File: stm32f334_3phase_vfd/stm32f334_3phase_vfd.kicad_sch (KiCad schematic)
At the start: 0 parts

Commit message: continue schematic work
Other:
- added sheet CPU (cpu.kicad_sch)
- sheet power ports: added 3V3_DIG, 3V3_ISENS, EM_STOP, HV, HinU, HinV, HinW, I_A, I_B, I_C, LinU, LinV, LinW, OUTPUT_PHA, OUTPUT_PHB, OUTPUT_PHC, T1, T2, Tso, VCC_15V; removed none

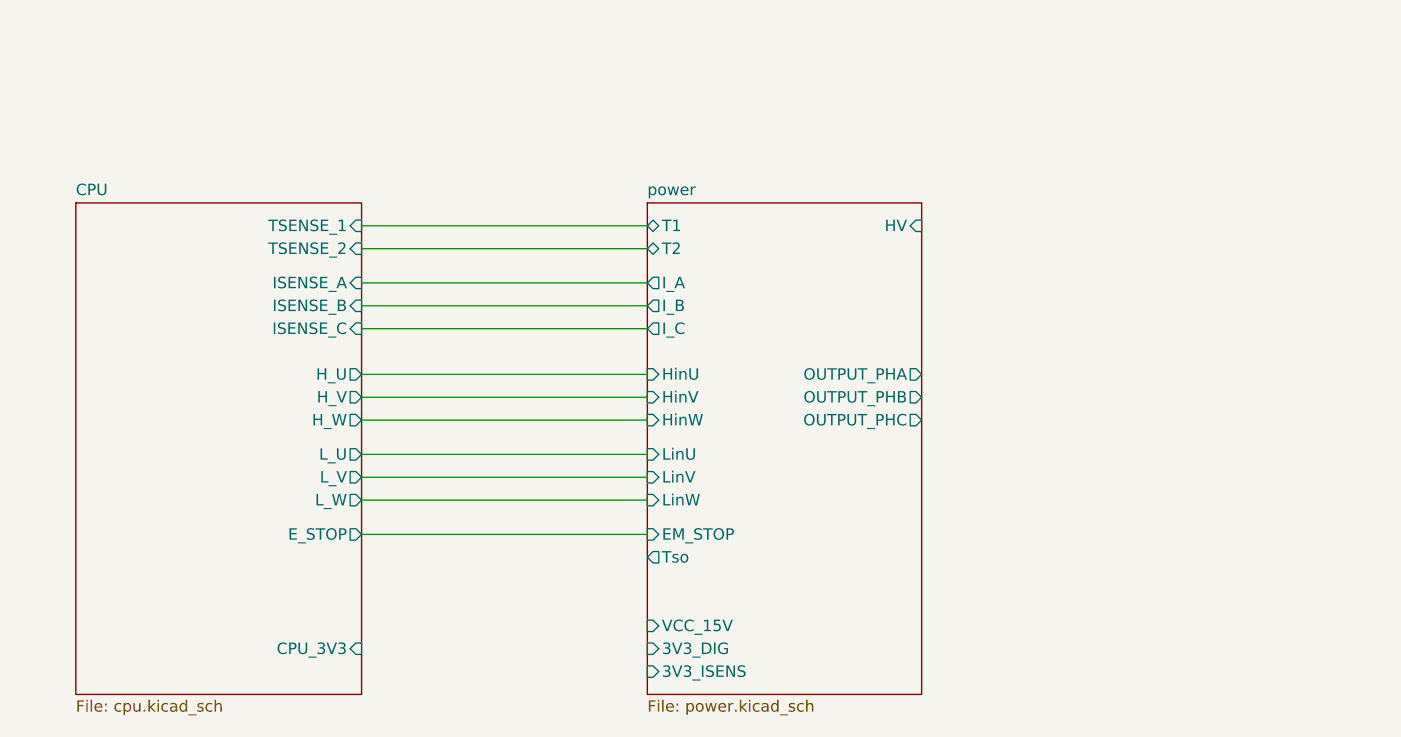
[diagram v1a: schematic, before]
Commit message: update schematic
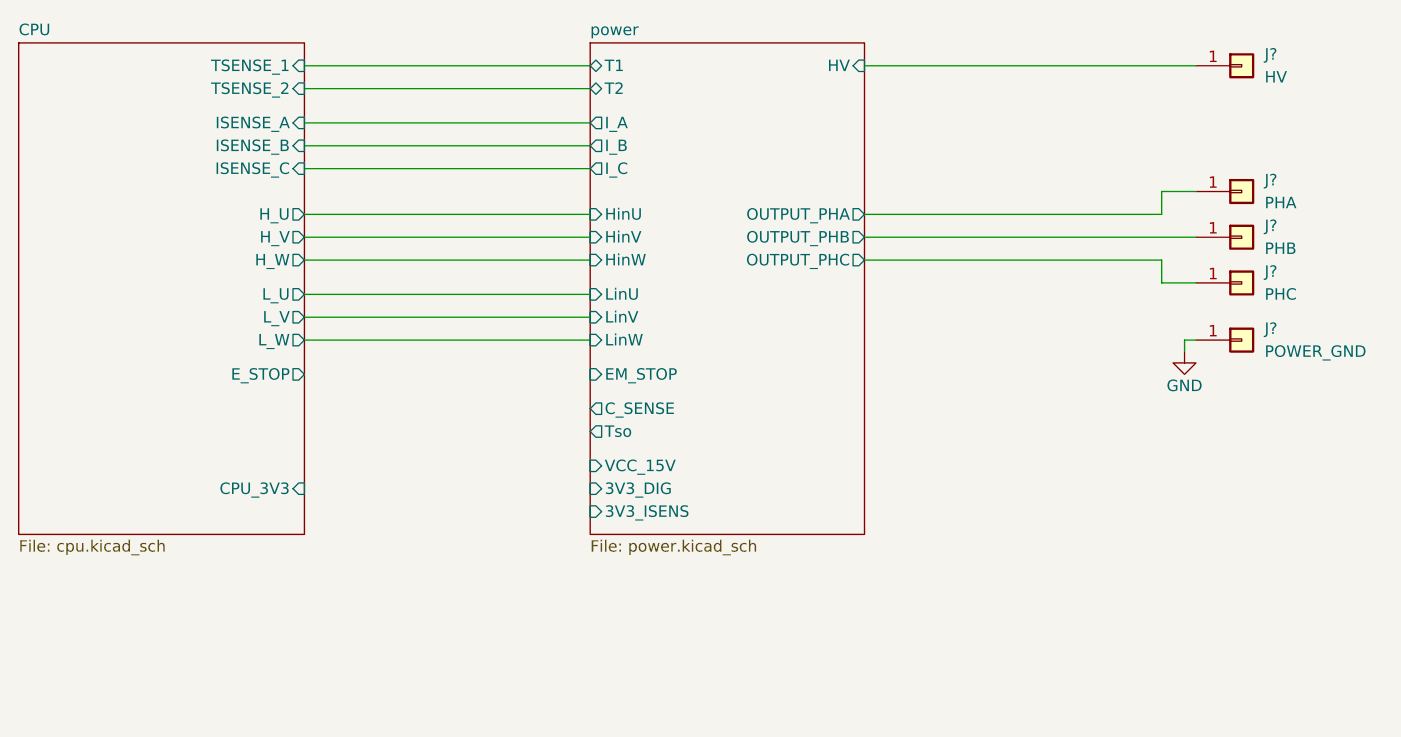
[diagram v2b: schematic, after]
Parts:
- added J?: PHB, symbol Connector_Generic:Conn_01x01
- added J?: PHA, symbol Connector_Generic:Conn_01x01
- added J?: HV, symbol Connector_Generic:Conn_01x01
- added J?: PHC, symbol Connector_Generic:Conn_01x01
- added J?: POWER_GND, symbol Connector_Generic:Conn_01x01
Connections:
- net power/HV: now also J?.1 (Pin_1)
- net power/OUTPUT_PHA: now also J?.1 (Pin_1)
- net power/OUTPUT_PHB: now also J?.1 (Pin_1)
- net power/OUTPUT_PHC: now also J?.1 (Pin_1)
- new net GND: J?.1 (Pin_1)
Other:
- sheet power ports: added C_SENSE; removed none

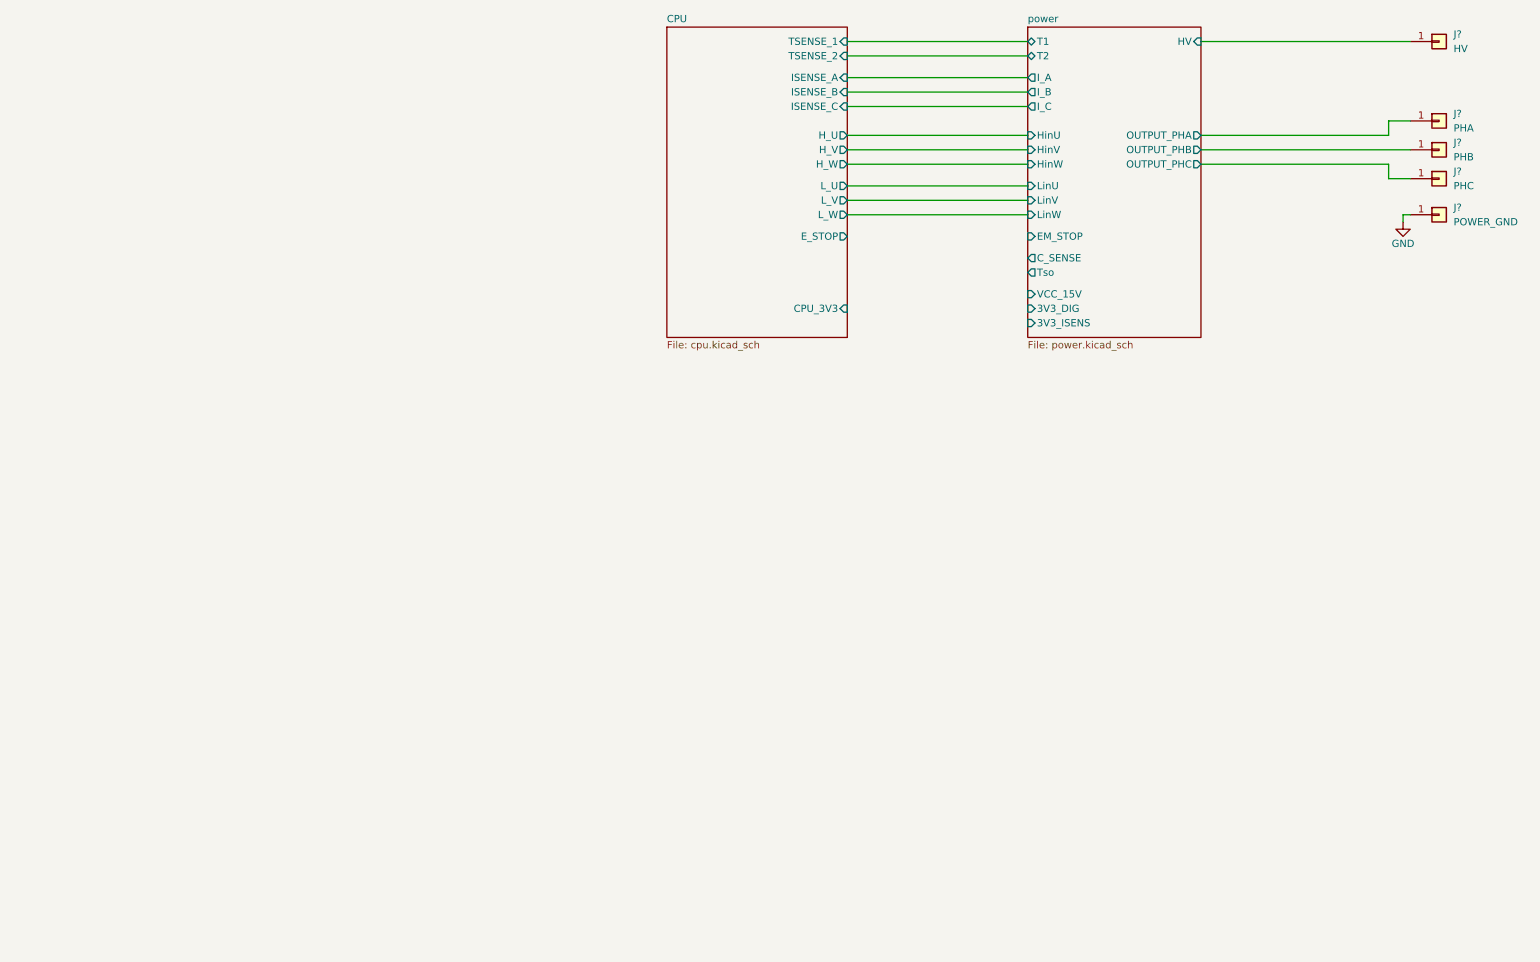
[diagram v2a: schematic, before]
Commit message: update schematic, start power section layout
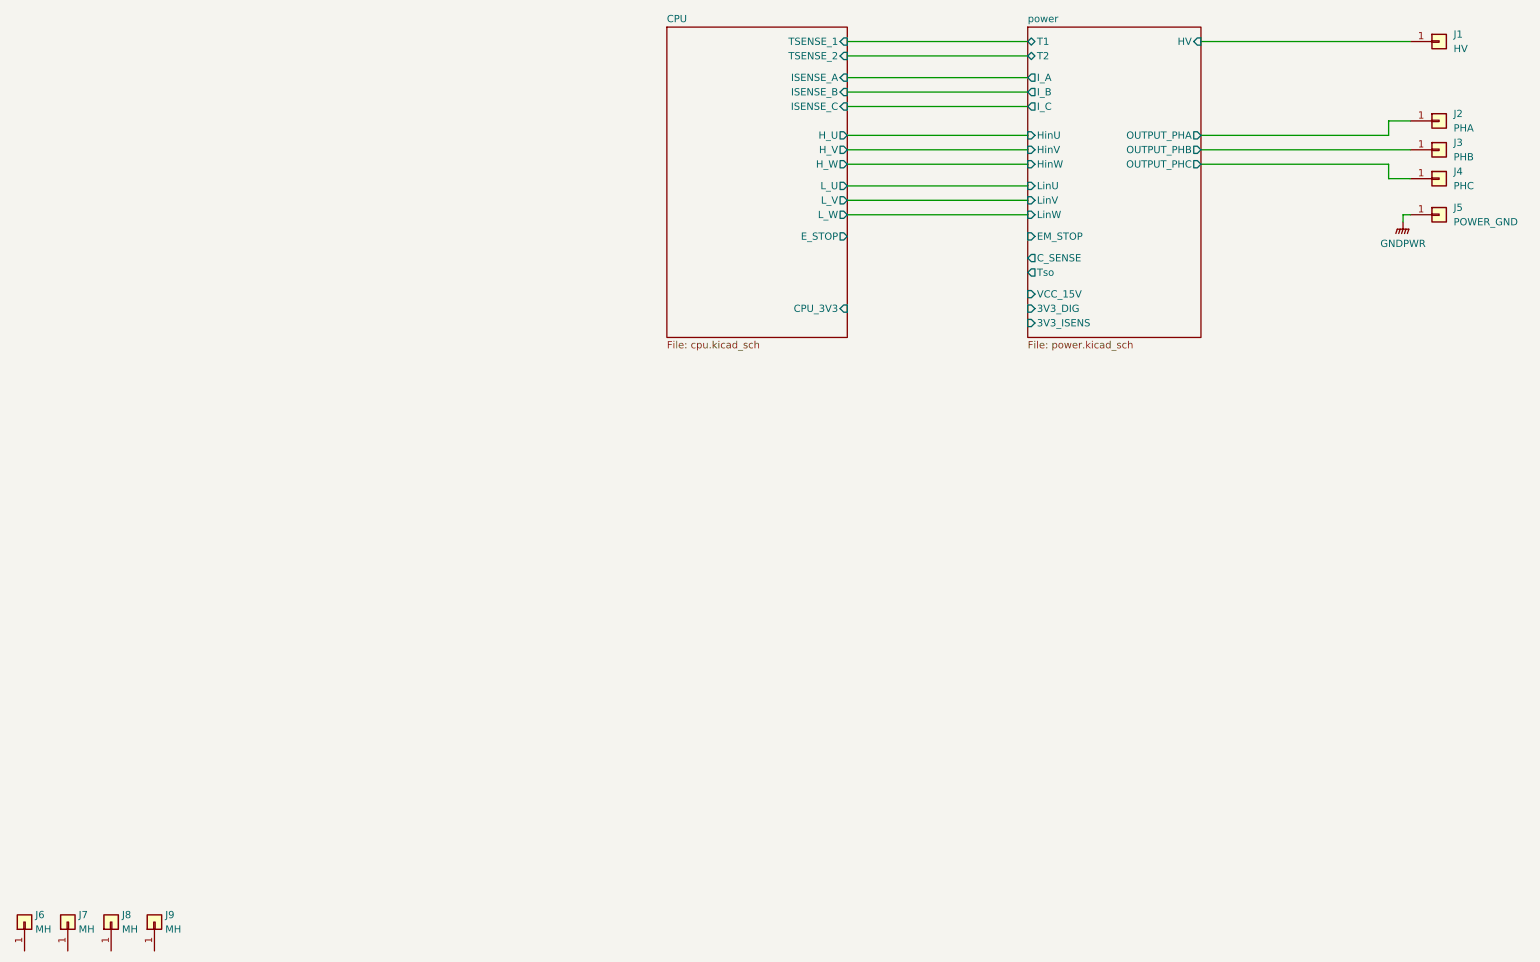
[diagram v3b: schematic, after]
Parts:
- added J6, J7, J8, J9: MH, MountingHole:MountingHole_3.2mm_M3_Pad_TopBottom, symbol Connector_Generic:Conn_01x01
- J1, J2, J3, J4, J5: renamed from J?; footprint (none) -> stm32f334_3phase_vfd:1904969
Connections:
- net GND renamed GNDPWR

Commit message: move 3 phase current sensors on a new board, allow for the current sense board to be stacked
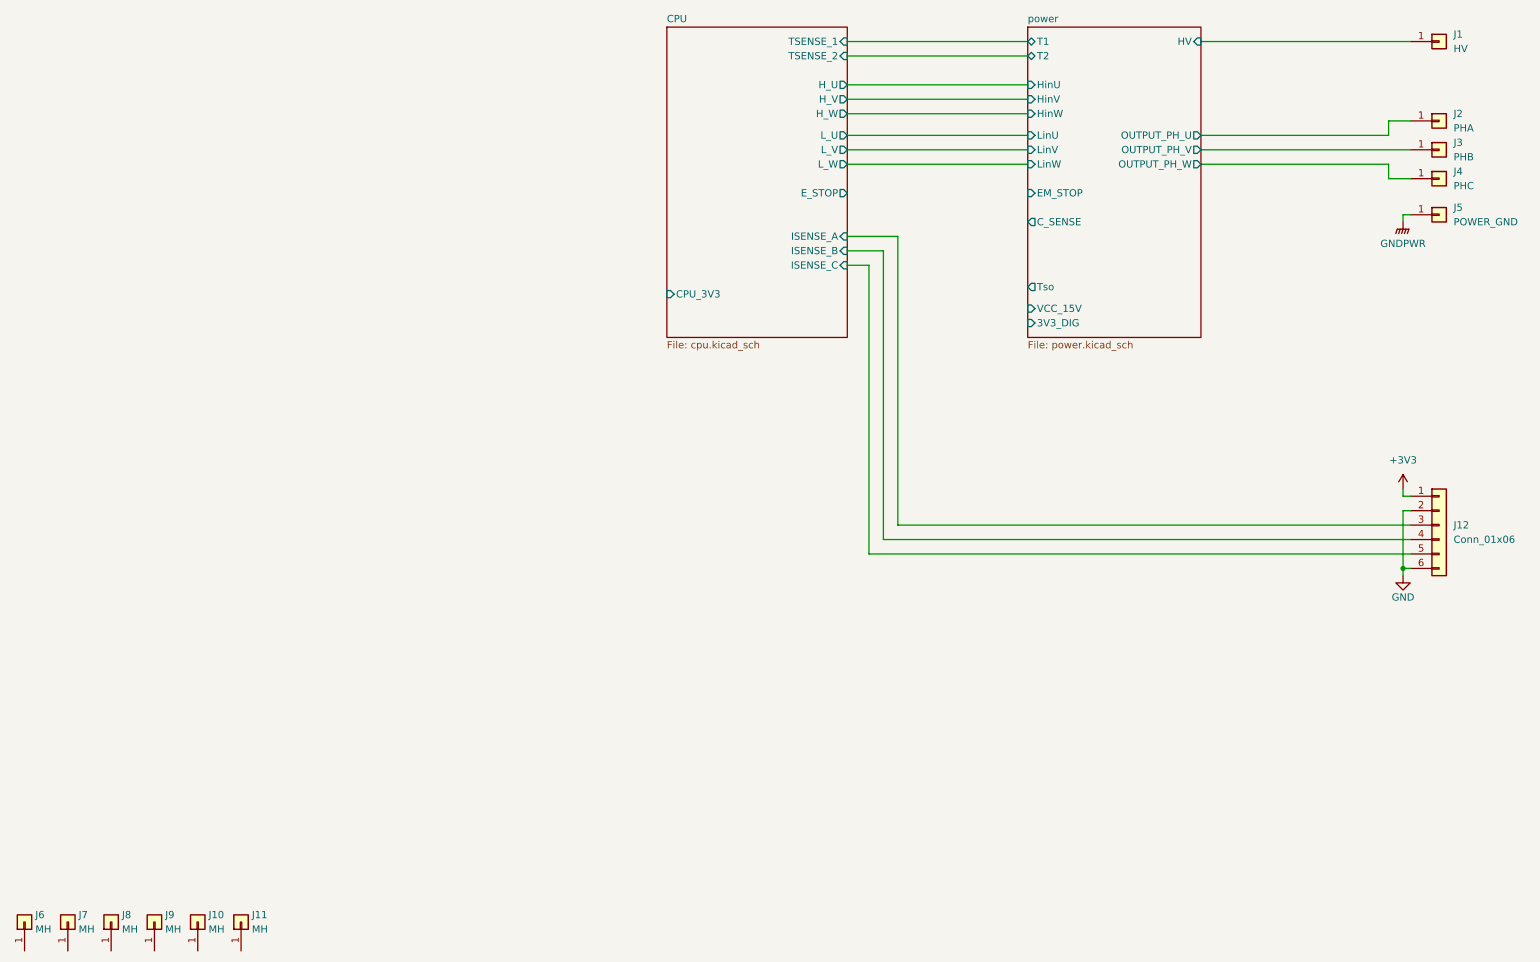
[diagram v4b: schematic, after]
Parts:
- added J10, J11: MH, MountingHole:MountingHole_3.2mm_M3_Pad_TopBottom, symbol Connector_Generic:Conn_01x01
- added J12: Conn_01x06, Connector_JST:JST_PH_B6B-PH-K_1x06_P2.00mm_Vertical, symbol Connector_Generic:Conn_01x06
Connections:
- net CPU/ISENSE_A: now also J12.3 (Pin_3)
- net CPU/ISENSE_B: now also J12.4 (Pin_4)
- net CPU/ISENSE_C: now also J12.5 (Pin_5)
- net power/OUTPUT_PHA renamed power/OUTPUT_PH_U
- net power/OUTPUT_PHB renamed power/OUTPUT_PH_V
- net power/OUTPUT_PHC renamed power/OUTPUT_PH_W
- new net +3V3: J12.1 (Pin_1)
- new net GND: J12.2 (Pin_2), J12.6 (Pin_6)
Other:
- sheet power ports: added OUTPUT_PH_U, OUTPUT_PH_V, OUTPUT_PH_W; removed 3V3_ISENS, I_A, I_B, I_C, OUTPUT_PHA, OUTPUT_PHB, OUTPUT_PHC

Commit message: switch to LQFP48 cpu, continue workin on layout
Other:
- sheet CPU ports: added C_SENSE; removed none
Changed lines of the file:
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@@
+    (stroke (width 0) (type default) (color 0 0 0 0))
+  )
+  (wire (pts (xy 163.83 53.34) (xy 195.58 53.34))
     (stroke (width 0) (type default) (color 0 0 0 0))
   )
@@
   (symbol (lib_id "power:+3V3") (at 261.62 100.33 0) (unit 1)
     (in_bom yes) (on_board yes) (fields_autoplaced)
-    (property "Reference" "#PWR?" (id 0) (at 261.62 104.14 0)
+    (property "Reference" "#PWR0108" (id 0) (at 261.62 104.14 0)
       (effects (font (size 1.27 1.27)) hide)
     )
@@
   (symbol (lib_id "power:GND") (at 261.62 115.57 0) (unit 1)
     (in_bom yes) (on_board yes)
-    (property "Reference" "#PWR?" (id 0) (at 261.62 121.92 0)
+    (property "Reference" "#PWR0109" (id 0) (at 261.62 121.92 0)
       (effects (font (size 1.27 1.27)) hide)
     )
@@
       (effects (font (size 1.27 1.27)) (justify right))
     )
+    (pin "C_SENSE" input (at 163.83 53.34 0)
+      (effects (font (size 1.27 1.27)) (justify right))
+    )
   )
   (sheet (at 195.58 19.05) (size 30.48 54.61) (fields_autoplaced)
@@
       (reference "#PWR0107") (unit 1) (value "GNDPWR") (footprint "")
     )
+    (path "/5688ef43-203d-42fa-8968-6c89131b4954"
+      (reference "#PWR0108") (unit 1) (value "+3V3") (footprint "")
+    )
+    (path "/ae8a7779-a204-40cc-a9a9-a5e8072c90c1"
+      (reference "#PWR0109") (unit 1) (value "GND") (footprint "")
+    )
+    (path "/6800bd5f-b25d-4977-8025-22368615975a/f68bf9a1-24c8-4c89-a68f-af7873d40121"
+      (reference "#PWR0110") (unit 1) (value "GND") (footprint "")
+    )
+    (path "/6800bd5f-b25d-4977-8025-22368615975a/08694d45-d770-4503-891f-e08473ebf295"
+      (reference "#PWR0111") (unit 1) (value "GND") (footprint "")
+    )
+    (path "/6800bd5f-b25d-4977-8025-22368615975a/ed269b40-9264-4042-b7e9-e49ce5a16a75"
+      (reference "#PWR0112") (unit 1) (value "GND") (footprint "")
+    )
+    (path "/6800bd5f-b25d-4977-8025-22368615975a/e9d903db-c5d7-444d-9c1e-bcca6f38ba00"
+      (reference "#PWR0113") (unit 1) (value "GND") (footprint "")
+    )
+    (path "/6800bd5f-b25d-4977-8025-22368615975a/c09010e8-cc9e-417f-b671-a1bfb5ab756d"
+      (reference "#PWR0114") (unit 1) (value "GND") (footprint "")
+    )
+    (path "/6800bd5f-b25d-4977-8025-22368615975a/f398151a-e08f-48fe-877f-4d66b9143ea6"
+      (reference "#PWR0115") (unit 1) (value "GND") (footprint "")
+    )
     (path "/aa6cee37-2fbc-47dd-b076-5b892a0ca157/9c4d5739-f999-44ba-9a82-45aeae16f88b"
       (reference "#PWR0201") (unit 1) (value "GND") (footprint "")
@@
       (reference "#PWR0223") (unit 1) (value "GNDPWR") (footprint "")
     )
-    (path "/5688ef43-203d-42fa-8968-6c89131b4954"
-      (reference "#PWR?") (unit 1) (value "+3V3") (footprint "")
-    )
-    (path "/ae8a7779-a204-40cc-a9a9-a5e8072c90c1"
-      (reference "#PWR?") (unit 1) (value "GND") (footprint "")
-    )
     (path "/6800bd5f-b25d-4977-8025-22368615975a/bb28fcff-49cf-47f9-96e8-a400a50b783f"
-      (reference "C101") (unit 1) (value "12p") (footprint "")
+      (reference "C101") (unit 1) (value "8p") (footprint "Capacitor_SMD:C_0805_2012Metric")
     )
     (path "/6800bd5f-b25d-4977-8025-22368615975a/3e6e72e2-2939-4642-a839-c8855147206b"
-      (reference "C102") (unit 1) (value "12p") (footprint "")
+      (reference "C102") (unit 1) (value "8p") (footprint "Capacitor_SMD:C_0805_2012Metric")
     )
     (path "/6800bd5f-b25d-4977-8025-22368615975a/2ded6777-98ae-4742-9048-0fb5127b8451"
@@
       (reference "C106") (unit 1) (value "100p") (footprint "")
     )
+    (path "/6800bd5f-b25d-4977-8025-22368615975a/7b383491-f576-4799-b6f2-d4cefc837494"
+      (reference "C107") (unit 1) (value "100n") (footprint "Capacitor_SMD:C_0805_2012Metric")
+    )
+    (path "/6800bd5f-b25d-4977-8025-22368615975a/55e1c19c-6471-4854-ae1e-a452d5d779ed"
+      (reference "C108") (unit 1) (value "100n") (footprint "Capacitor_SMD:C_0805_2012Metric")
+    )
+    (path "/6800bd5f-b25d-4977-8025-22368615975a/6b23bf18-b0b1-4a63-82f9-3b27a3f9e805"
+      (reference "C109") (unit 1) (value "100n") (footprint "Capacitor_SMD:C_0805_2012Metric")
+    )
+    (path "/6800bd5f-b25d-4977-8025-22368615975a/46fb485b-9078-4658-a2cc-ac368a97ae6a"
+      (reference "C110") (unit 1) (value "100n") (footprint "Capacitor_SMD:C_0805_2012Metric")
+    )
+    (path "/6800bd5f-b25d-4977-8025-22368615975a/8c1b7f52-2e43-40f0-b428-ca9c61779ace"
+      (reference "C111") (unit 1) (value "100n") (footprint "Capacitor_SMD:C_0805_2012Metric")
+    )
     (path "/aa6cee37-2fbc-47dd-b076-5b892a0ca157/852a89ef-a6e3-470b-bcac-92bad7c31bee"
       (reference "C201") (unit 1) (value "10p") (footprint "Capacitor_SMD:C_1206_3216Metric")
     )
     (path "/aa6cee37-2fbc-47dd-b076-5b892a0ca157/e770c8e0-8aef-44ba-b471-bdda9480f84f"
-      (reference "C202") (unit 1) (value "330nF/630V") (footprint "Capacitor_THT:C_Rect_L24.0mm_W10.1mm_P22.50mm_MKT")
+      (reference "C202") (unit 1) (value "B32774X8305K000") (footprint "Capacitor_THT:C_Rect_L31.5mm_W11.0mm_P27.50mm_MKS4")
     )
     (path "/aa6cee37-2fbc-47dd-b076-5b892a0ca157/bbb37b50-37ae-4186-9cec-6d30ec0636e9"
@@
       (reference "J218") (unit 1) (value "TP_CSENSE") (footprint "Connector_PinHeader_2.54mm:PinHeader_1x01_P2.54mm_Vertical")
     )
+    (path "/6800bd5f-b25d-4977-8025-22368615975a/a2f2506b-84f1-4757-8c2e-6bff34315fbf"
+      (reference "L101") (unit 1) (value "FB") (footprint "Inductor_SMD:L_0805_2012Metric")
+    )
     (path "/6800bd5f-b25d-4977-8025-22368615975a/e0ba799e-69ee-49fa-ac70-0ad7f3dd2e9e"
       (reference "R101") (unit 1) (value "100") (footprint "")
@@
       (reference "R217") (unit 1) (value "0") (footprint "Resistor_SMD:R_0805_2012Metric")
     )
-    (path "/6800bd5f-b25d-4977-8025-22368615975a/ab1e31e7-0e6f-420c-ae17-560fc4649a7a"
-      (reference "U101") (unit 1) (value "STM32F334K6Tx") (footprint "Package_QFP:LQFP-32_7x7mm_P0.8mm")
+    (path "/6800bd5f-b25d-4977-8025-22368615975a/005851cc-e359-44c9-ae09-f28bb43db3f8"
+      (reference "U100") (unit 1) (value "STM32F334C8Tx") (footprint "Package_QFP:LQFP-48_7x7mm_P0.5mm")
+    )
+    (path "/6800bd5f-b25d-4977-8025-22368615975a/d5b7e7ab-6e3b-413e-9f79-67ea7ccc8745"
+      (reference "U101") (unit 1) (value "ECS-160-10-36-CKM-TR3") (footprint "Crystal:Crystal_SMD_2520-4Pin_2.5x2.0mm")
     )
     (path "/aa6cee37-2fbc-47dd-b076-5b892a0ca157/65cb261d-2cec-4a04-842e-1fc90ef50d41"
       (reference "U201") (unit 1) (value "STGIB15CH60TS-L") (footprint "stm32f334_3phase_vfd:SDIP2B-26L_L1_STM")
     )
-    (path "/6800bd5f-b25d-4977-8025-22368615975a/f380355e-e2bf-4cca-95fe-8cfaa76428f3"
-      (reference "Y101") (unit 1) (value "Crystal_Small") (footprint "")
-    )
-  )
+  )
